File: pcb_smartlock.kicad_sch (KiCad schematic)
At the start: 59 parts, among them IC1 ST25R3918-AQET, J1 Conn_01x02, J2 Conn_01x03, Q3 IRLML6344TRPBF, Q4 IRLML6344TRPBF, U2 SPX3819M5-L-1-8, U3 ESP32-C3-MINI-1-H4X, U5 SPX3819M5-L-1-8

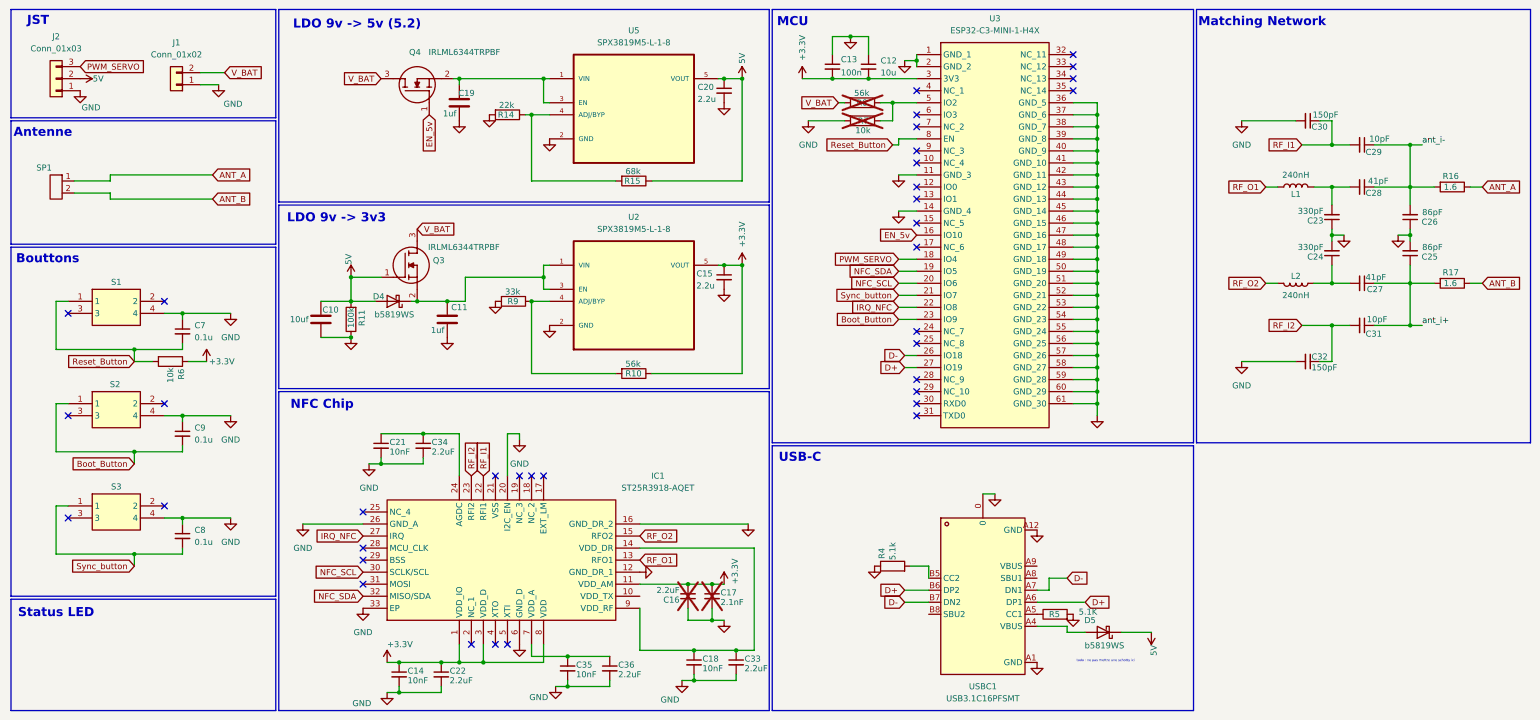
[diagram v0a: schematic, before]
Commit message: Finition PCB des boutons
J'ai relié chacun des 3 boutons à leur source de tension et à un GND.
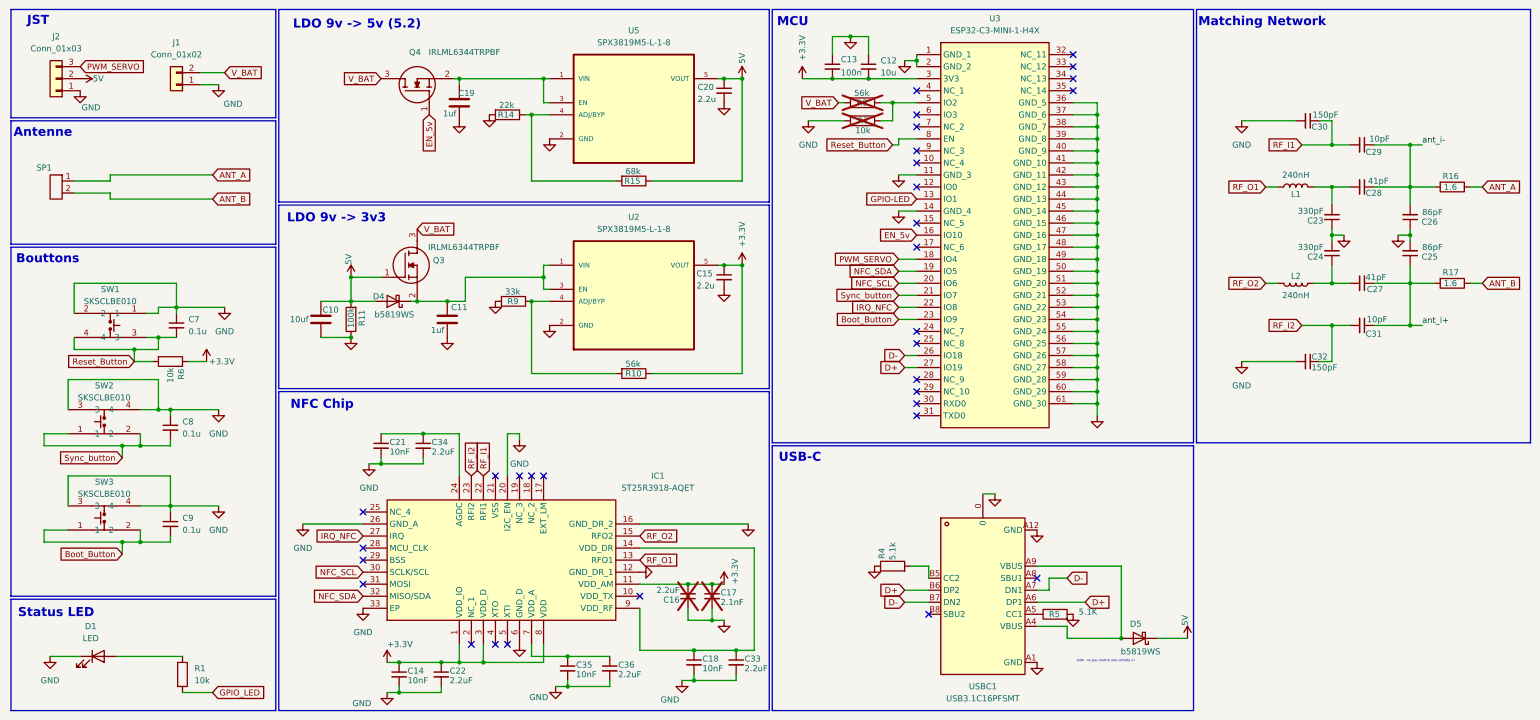
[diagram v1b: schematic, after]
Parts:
- removed S1, S2, S3: PTS810SJM250SMTRLFS, PTS810SJM250SMTRLFS:PTS810SJG250SMTRLFS, symbol PTS810SJM250SMTRLFS:PTS810SJM250SMTRLFS
- added D1: LED, LED_SMD:LED_0603_1608Metric, symbol Device:LED
- added R1: 10k, Resistor_SMD:R_0603_1608Metric, symbol Device:R
- added SW1, SW2, SW3: SKSCLBE010, SKSCLBE010:KEY-SMD_4P-SKSCLXX010, symbol SKSCLBE010:SKSCLBE010
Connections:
- net Boot_Button: now also SW3.1, SW3.2
- net GND: now also D1.1 (K), SW1.1, SW1.2, SW2.3, SW2.4, SW3.3, SW3.4
- net Reset_Button: now also SW1.3, SW1.4
- net Sync_button: now also SW2.1, SW2.2
- net at D5.2 (A), USBC1.A4 (VBUS): now also USBC1.A9 (VBUS)
- net GPIO-LED: now reaches U3.13 (IO1)
- new net: D1.2 (A), R1.1
- new net GPIO_LED: R1.2
- no-connect marks 36 -> 32
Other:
- moved on the sheet: C7, C8, C9, D5

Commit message: Fix most of routing
TODO : silkscreen
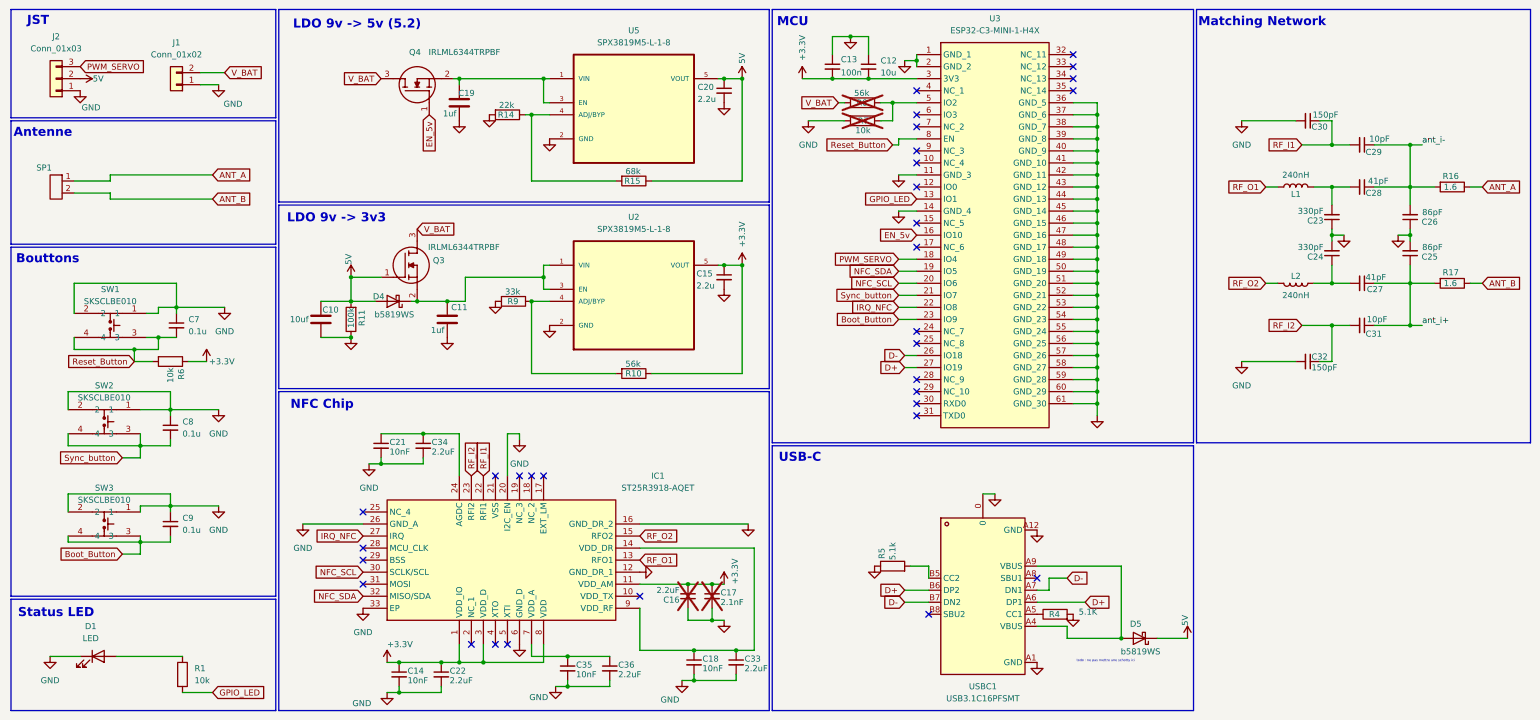
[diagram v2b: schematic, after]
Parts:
- renumbered R5 to R4, R4 to R5
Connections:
- net GPIO-LED is gone; now on net GPIO_LED: U3.13 (IO1)
- net Boot_Button: now also SW3.3, SW3.4; no longer SW3.1, SW3.2
- net GND: now also SW2.1, SW2.2, SW3.1, SW3.2; no longer SW2.3, SW2.4, SW3.3, SW3.4
- net Sync_button: now also SW2.3, SW2.4; no longer SW2.1, SW2.2
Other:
- moved on the sheet: SW2, SW3
